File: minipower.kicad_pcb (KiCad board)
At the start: 2 copper layers, 101.3 x 26.9 mm, 24 parts

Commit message: add graphic
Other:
- board text added: "IP5306 21700 mini powerbank/charger rev 2 by Kevin Goh"
- board text removed: "IP5306 21700 mini powerbank/charger rev 1 by Kevin Goh"

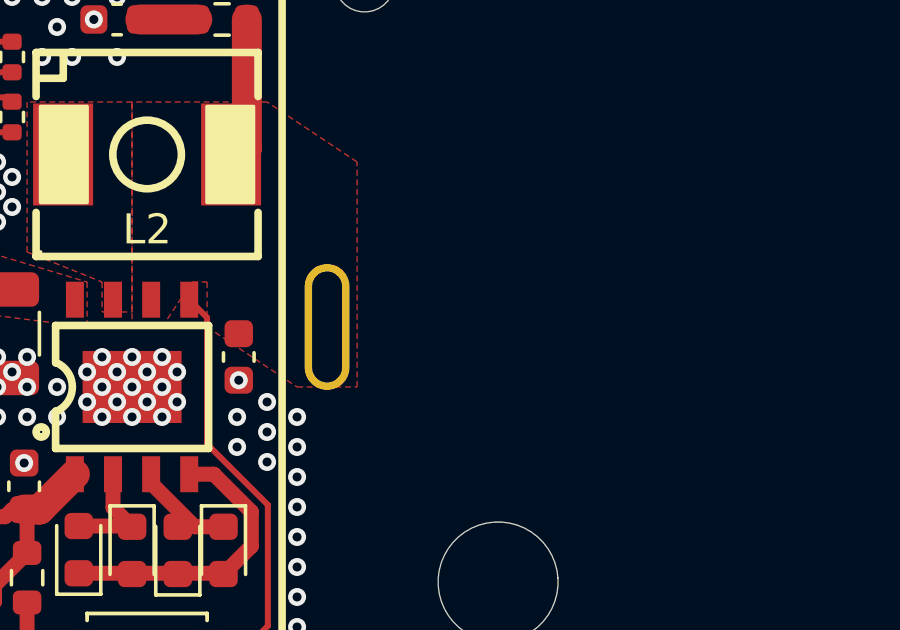
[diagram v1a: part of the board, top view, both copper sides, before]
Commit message: cleaning up
some changes to graphics, had mental breakdown over how to source battery holders
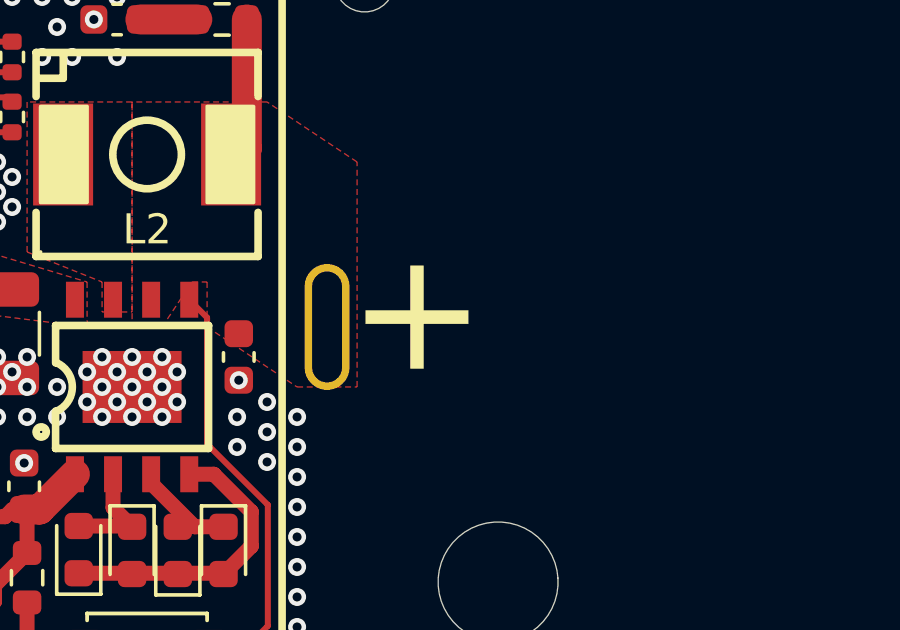
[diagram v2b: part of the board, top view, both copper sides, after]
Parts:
- added REF**: Burden_Bear_40, PCBWorkshop_2026_footprints:Burden_Bear_40, B.Cu at (190.4, 67.1)
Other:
- board text added: "+"
- board text added: "EIG PCB Workshop 2026"
- board text removed: "+5V OUT"
